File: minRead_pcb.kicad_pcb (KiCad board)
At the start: 2 copper layers, 133.9 x 116.2 mm, 121 parts, among them J1 USB_C_Receptacle, J2 FH34SRJ-24S-0.5SH_50_, J3 FH34SRJ-6S-0.5SH_50_, J5 Conn_01x02, J7 Micro_SD_Card, Q10 BSS138, Q11 BSS138, Q16 MMBT3906, Q17 MMBT3904, Q18 AO3419, Q4 [BSS138] AO3400A, Q5 AO3419, SW1 SW_Push, SW10 SW_Push, SW11 SW_Push, SW2 SW_Push, SW3 SW_Push, SW4 SW_Push, SW6 SW_Push, SW8 SW_Push, SW9 SW_Push, U1 TPD4E1U06DBVR, U11 AP3031KTR, U2 TPS2116DRL, U3 AP2112K-3.3, U4 ESP32-S3-WROOM-1, U6 TPD4E1U06DBVR, U7 MCP73832-2-OT

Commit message: general setup prep for routing
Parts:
- moved J1 133.1 mm to (92.5, 39.7), turned to 0 degrees
- moved J7 114.1 mm to (93.9, 133.2), turned to -90 degrees
- moved U4 102.6 mm to (59.2, 47.7), turned to -135 degrees
- moved R21 99.5 mm to (48.7, 55.9), turned to -135 degrees
- moved R22 98.0 mm to (50.2, 57.4), turned to -135 degrees
- moved R23 96.5 mm to (51.7, 58.9), turned to -135 degrees
- moved R25 95.0 mm to (53.2, 60.4), turned to -135 degrees
- moved R29 94.5 mm to (74.9, 54.5), turned to 135 degrees
- moved R30 93.7 mm to (73.5, 55.9), turned to 135 degrees
- moved R24 93.5 mm to (54.7, 61.9), turned to -135 degrees
- moved R31 93.0 mm to (72.0, 57.2), turned to 135 degrees
- moved R32 92.1 mm to (70.7, 58.7), turned to 135 degrees
- moved R13 91.3 mm to (56.9, 64.1), turned to 45 degrees
- moved R33 91.3 mm to (69.2, 60.1), turned to 135 degrees
- moved R34 90.6 mm to (67.8, 61.5), turned to 135 degrees
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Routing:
- net Net-(U4-IO42): track 0.00 -> 4.34 mm
- net Net-(U4-IO41): track 0.00 -> 3.93 mm
- net ESP32_IO0: track 0.00 -> 3.68 mm
- net Net-(U4-IO40): track 0.00 -> 3.57 mm
- net Net-(U4-IO38): track 0.00 -> 3.43 mm
- net Net-(U4-IO39): track 0.00 -> 3.22 mm
- net Net-(U4-IO9): track 0.00 -> 3.07 mm
- net Net-(U4-IO14): track 0.00 -> 2.96 mm
- net Net-(U4-IO10): track 0.00 -> 2.72 mm
- net Net-(U4-IO13): track 0.00 -> 2.66 mm
- net Net-(U4-IO12): track 0.00 -> 2.35 mm
- net Net-(U4-IO11): track 0.00 -> 2.31 mm
- net Net-(U4-IO48): track 0.00 -> 2.06 mm
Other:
- board size 133.9 x 116.2 mm -> 151.5 x 148.6 mm

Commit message: add specific netclasses
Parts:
- moved R7 102.2 mm to (67.8, 55.6), turned to 90 degrees
- moved C5 100.7 mm to (70.0, 55.6), turned to -90 degrees
- moved C32 100.4 mm to (66.2, 58.6), turned to 0 degrees
- moved C33 99.2 mm to (62.4, 58.6)
- moved R29 18.7 mm to (72.2, 36.0), turned to 180 degrees
- moved R30 17.9 mm to (72.2, 38.0), turned to 180 degrees
- moved R31 17.2 mm to (72.1, 40.0), turned to 180 degrees
- moved R32 16.8 mm to (72.2, 42.0), turned to 180 degrees
- moved R33 16.4 mm to (72.2, 44.0), turned to 180 degrees
- moved R34 16.1 mm to (72.2, 46.0), turned to 180 degrees
- moved R26 15.8 mm to (72.0, 48.2), turned to 0 degrees
- moved R13 12.1 mm to (65.4, 55.5), turned to 90 degrees
- moved R24 10.6 mm to (63.2, 55.5), turned to -90 degrees
- moved R25 9.24 mm to (61.1, 55.5), turned to -90 degrees
- moved R23 7.97 mm to (59.0, 55.5), turned to -90 degrees
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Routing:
- net 3V3: track 0.00 -> 39.3 mm, vias 0 -> 2
- net ESP32_EN: track 0.00 -> 35.2 mm, vias 0 -> 2
- net ESP32_IO0: track 3.68 -> 4.20 mm

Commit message: implement charge pump
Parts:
- removed C25, C26: 1u, Capacitor_SMD:C_0805_2012Metric_Pad1.18x1.45mm_HandSolder
- removed C4: 22u, Capacitor_SMD:C_0805_2012Metric_Pad1.18x1.45mm_HandSolder
- removed R38: 310k, Resistor_SMD:R_0805_2012Metric_Pad1.20x1.40mm_HandSolder
- removed R51, R58: 100k, Resistor_SMD:R_0805_2012Metric_Pad1.20x1.40mm_HandSolder
- removed U2: TPS2116DRL, Package_TO_SOT_SMD:SOT-583-8
- added C7: 22u, Capacitor_SMD:C_0805_2012Metric_Pad1.18x1.45mm_HandSolder, B.Cu at (94.0, 55.0)
- added C9: 4.7u, Capacitor_SMD:C_0805_2012Metric_Pad1.18x1.45mm_HandSolder, B.Cu at (86.2, 53.6)
- added D7: B5819W, Diode_SMD:D_SOD-123, B.Cu at (89.8, 56.2)
- added Q6: AO3419, Package_TO_SOT_SMD:SOT-23_Handsoldering, B.Cu at (85.4, 56.6)
- added R67: 100k, Resistor_SMD:R_0805_2012Metric_Pad1.20x1.40mm_HandSolder, B.Cu at (92.0, 55.0)
- J5: footprint Connector_JST:JST_PH_S2B-PH-K_1x02_P2.00mm_Horizontal -> DEAN:Battery pads
- moved C19 163.4 mm to (71.6, 132.6), turned to 90 degrees
- moved C18 160.6 mm to (69.6, 132.6), turned to 90 degrees
- moved C14 159.4 mm to (75.6, 132.6), turned to 90 degrees
- moved C17 156.1 mm to (65.6, 132.6), turned to 90 degrees
- moved R14 153.5 mm to (76.8, 156.4)
- moved C20 151.6 mm to (81.6, 132.6), turned to 90 degrees
- moved C16 151.0 mm to (79.6, 132.6), turned to 90 degrees
- moved Q4 150.5 mm to (74.0, 156.5), turned to -90 degrees
- moved C15 150.5 mm to (77.6, 132.6), turned to 90 degrees
- moved R15 150.0 mm to (71.2, 156.6)
- moved C13 148.4 mm to (73.6, 132.6), turned to 90 degrees
- moved C6 146.5 mm to (96.2, 59.2), turned to 90 degrees
- moved R12 141.2 mm to (73.8, 57.1), turned to 90 degrees
- moved L1 139.8 mm to (68.0, 156.6)
- moved U3 139.4 mm to (93.4, 59.8), turned to -90 degrees
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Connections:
- U4 pad 6: WARM_TOGGLE -> COLOR_SEL
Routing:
- net BAT_MONIT: track 0.00 -> 34.6 mm
- net ESP32_EN: track 35.2 -> 2.22 mm, vias 2 -> 0
- net P+: track 0.00 -> 25.0 mm
- net B-: track 0.00 -> 24.1 mm, vias 0 -> 1
- net LDO_IN: track 0.00 -> 11.1 mm
- net Net-(C18-Pad2): track 0.00 -> 10.7 mm
- net 3V3: track 39.3 -> 49.6 mm
- net USB_VBUS: track 0.00 -> 9.89 mm
- net Net-(D5-A): track 0.00 -> 9.18 mm
- net Net-(C19-Pad2): track 0.00 -> 9.17 mm
- net Net-(C13-Pad2): track 0.00 -> 7.70 mm
- net Net-(C17-Pad2): track 0.00 -> 7.61 mm
- net Net-(C20-Pad2): track 0.00 -> 7.34 mm
- net /PREVGH: track 0.00 -> 6.40 mm
- net Net-(D4-K): track 0.00 -> 6.00 mm
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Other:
- outline, holes or cut-outs redrawn

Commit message: charge pump in place
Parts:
- moved R15 22.5 mm to (83.0, 137.4)
- moved C10 20.0 mm to (71.2, 137.6)
- moved D6 20.0 mm to (62.2, 138.0)
- moved L1 20.0 mm to (74.4, 137.6)
- moved C11 20.0 mm to (66.8, 138.0)
- moved D4 20.0 mm to (64.6, 138.0)
- moved D5 20.0 mm to (69.0, 137.8)
- moved Q4 19.4 mm to (78.2, 137.5)
- moved R14 19.4 mm to (81.0, 137.4)
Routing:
- net /GDR: track 1.85 -> 6.65 mm
- net Net-(D5-A): track 9.18 -> 5.43 mm
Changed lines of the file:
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@@
 	(footprint "Capacitor_SMD:C_0805_2012Metric_Pad1.18x1.45mm_HandSolder"
 		(layer "B.Cu")
-		(at 64.8 156.5625 -90)
+		(at 71.2 137.6 -90)
 		(descr "Capacitor SMD 0805 (2012 Metric), square (rectangular) end terminal, IPC-7351 nominal with elongated pad for handsoldering. (Body size source: IPC-SM-782 page 76, https://www.pcb-3d.com/wordpress/wp-content/uploads/ipc-sm-782a_amendment_1_and_2.pdf, https://docs.google.com/spreadsheets/d/1BsfQQcO9C6DZCsRaXUlFlo91Tg2WpOkGARC1WS5S8t0/edit?usp=sharing), generated with kicad-footprint-generator")
 		(tags "capacitor handsolder")
@@
 	(footprint "Capacitor_SMD:C_0805_2012Metric_Pad1.18x1.45mm_HandSolder"
 		(layer "B.Cu")
-		(at 60.4 156.9625 -90)
+		(at 66.8 138 -90)
 		(descr "Capacitor SMD 0805 (2012 Metric), square (rectangular) end terminal, IPC-7351 nominal with elongated pad for handsoldering. (Body size source: IPC-SM-782 page 76, https://www.pcb-3d.com/wordpress/wp-content/uploads/ipc-sm-782a_amendment_1_and_2.pdf, https://docs.google.com/spreadsheets/d/1BsfQQcO9C6DZCsRaXUlFlo91Tg2WpOkGARC1WS5S8t0/edit?usp=sharing), generated with kicad-footprint-generator")
 		(tags "capacitor handsolder")
@@
 	(footprint "Package_TO_SOT_SMD:SOT-23"
 		(layer "B.Cu")
-		(at 74 156.5 -90)
+		(at 78.2 137.5375 -90)
 		(descr "SOT, 3 Pin (JEDEC TO-236 Var AB https://www.jedec.org/document_search?search_api_views_fulltext=TO-236), generated with kicad-footprint-generator ipc_gullwing_generator.py")
 		(tags "SOT TO_SOT_SMD")
@@
 	(footprint "Resistor_SMD:R_0805_2012Metric_Pad1.20x1.40mm_HandSolder"
 		(layer "B.Cu")
-		(at 71.2 156.5625 90)
+		(at 83 137.4375 90)
 		(descr "Resistor SMD 0805 (2012 Metric), square (rectangular) end terminal, IPC-7351 nominal with elongated pad for handsoldering. (Body size source: IPC-SM-782 page 72, https://www.pcb-3d.com/wordpress/wp-content/uploads/ipc-sm-782a_amendment_1_and_2.pdf), generated with kicad-footprint-generator")
 		(tags "resistor handsolder")
@@
 	(footprint "Diode_SMD:D_SOD-123"
 		(layer "B.Cu")
-		(at 55.8 156.9625 -90)
+		(at 62.2 138 -90)
 		(descr "SOD-123")
 		(tags "SOD-123")
@@
 	(footprint "Diode_SMD:D_SOD-123"
 		(layer "B.Cu")
-		(at 62.6 156.7625 -90)
+		(at 69 137.8 -90)
 		(descr "SOD-123")
 		(tags "SOD-123")
@@
 	(footprint "Resistor_SMD:R_0805_2012Metric_Pad1.20x1.40mm_HandSolder"
 		(layer "B.Cu")
-		(at 76.8 156.3625 90)
+		(at 81 137.4375 90)
 		(descr "Resistor SMD 0805 (2012 Metric), square (rectangular) end terminal, IPC-7351 nominal with elongated pad for handsoldering. (Body size source: IPC-SM-782 page 72, https://www.pcb-3d.com/wordpress/wp-content/uploads/ipc-sm-782a_amendment_1_and_2.pdf), generated with kicad-footprint-generator")
 		(tags "resistor handsolder")
@@
 	(footprint "Diode_SMD:D_SOD-123"
 		(layer "B.Cu")
-		(at 58.2 156.9625 90)
+		(at 64.6 138 90)
 		(descr "SOD-123")
 		(tags "SOD-123")
@@
 	(footprint "srn3010C-100m:IND_SRN3010C-100M"
 		(layer "B.Cu")
-		(at 68 156.5625 180)
+		(at 74.4 137.6 180)
 		(property "Reference" "L1"
 			(at 0 2.25 0)
@@
 	)
 	(segment
-		(start 64.8 157.6)
-		(end 65.8625 157.6)
+		(start 71.2 138.6375)
+		(end 72.2625 138.6375)
 		(width 0.5)
 		(layer "B.Cu")
@@
 	)
 	(segment
-		(start 65.8625 157.6)
-		(end 66.9 156.5625)
+		(start 72.2625 138.6375)
+		(end 73.3 137.6)
 		(width 0.5)
 		(layer "B.Cu")
@@
 	)
 	(segment
-		(start 60.4 155.925)
-		(end 58.2 158.125)
+		(start 66.8 136.9625)
+		(end 64.6 139.1625)
 		(width 0.5)
 		(layer "B.Cu")
@@
 	)
 	(segment
-		(start 58.2 158.125)
-		(end 58.2 158.6125)
+		(start 64.6 139.1625)
+		(end 64.6 139.65)
 		(width 0.5)
 		(layer "B.Cu")
@@
 	)
 	(segment
-		(start 55.8 158.6125)
-		(end 58.2 158.6125)
+		(start 62.2 139.65)
+		(end 64.6 139.65)
 		(width 0.5)
 		(layer "B.Cu")
@@
 	)
 	(segment
-		(start 62.6 158.4125)
-		(end 60.8125 158.4125)
+		(start 69 139.45)
+		(end 67.2125 139.45)
 		(width 0.5)
 		(layer "B.Cu")
@@
 	)
 	(segment
-		(start 60.8125 158.4125)
-		(end 60.4 158)
+		(start 67.2125 139.45)
+		(end 66.8 139.0375)
 		(width 0.5)
 		(layer "B.Cu")
@@
 	)
 	(segment
-		(start 69.1 157.400798)
-		(end 69.1 156.5625)
+		(start 76.375 138.475)
+		(end 78.2 138.475)
 		(width 0.5)
 		(layer "B.Cu")
@@
 	)
 	(segment
-		(start 72.725 158.7125)
-		(end 70.411702 158.7125)
-		(width 0.5)
-		(layer "B.Cu")
-		(net "Net-(D5-A)")
-	)
-	(segment
-		(start 70.411702 158.7125)
-		(end 69.1 157.400798)
-		(width 0.5)
-		(layer "B.Cu")
-		(net "Net-(D5-A)")
-	)
-	(segment
-		(start 74 157.4375)
-		(end 72.725 158.7125)
+		(start 75.5 137.6)
+		(end 76.375 138.475)
 		(width 0.5)
 		(layer "B.Cu")
@@
 	)
 	(segment
-		(start 73.05 155.5625)
-		(end 71.2 155.5625)
+		(start 78.4125 135.4375)
+		(end 77.25 136.6)
+		(width 0.2)
+		(layer "B.Cu")
+		(net "/GDR")
+	)
+	(segment
+		(start 83 136.4375)
+		(end 82 135.4375)
+		(width 0.2)
+		(layer "B.Cu")
+		(net "/GDR")
+	)
+	(segment
+		(start 82 135.4375)
+		(end 78.4125 135.4375)
 		(width 0.2)
 		(layer "B.Cu")
@@
 	)
 	(segment
-		(start 76.8 155.3625)
-		(end 75.15 155.3625)
+		(start 81 136.4)
+		(end 79.35 136.4)
 		(width 0.5)
 		(layer "B.Cu")
@@
 	)
 	(segment
-		(start 75.15 155.3625)
-		(end 74.95 155.5625)
+		(start 79.35 136.4)
+		(end 79.15 136.6)
 		(width 0.5)
 		(layer "B.Cu")

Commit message: light bar circuit mostly routed
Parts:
- moved R48 257.9 mm to (49.0, 137.8), turned to -90 degrees
- moved R47 249.2 mm to (57.9, 138.1), turned to -90 degrees
- moved Q17 245.0 mm to (51.7, 137.0), turned to 90 degrees
- moved Q16 241.4 mm to (55.2, 137.0), turned to 90 degrees
- moved R63 180.4 mm to (49.9, 132.3), turned to -90 degrees
- moved R62 174.9 mm to (58.7, 132.3), turned to -90 degrees
- moved C30 170.7 mm to (59.1, 135.2), turned to 0 degrees
- moved Q10 163.9 mm to (56.0, 132.3), turned to 90 degrees
- moved Q11 163.8 mm to (52.5, 132.3), turned to 90 degrees
- moved R65 154.7 mm to (47.2, 66.4)
- moved C34 151.9 mm to (44.4, 61.9), turned to 90 degrees
- moved R64 150.9 mm to (51.3, 64.6)
- moved C31 147.8 mm to (48.4, 58.0), turned to -90 degrees
- moved R5 146.4 mm to (65.6, 132.6), turned to -90 degrees
- moved Q18 144.3 mm to (47.2, 62.7), turned to 90 degrees
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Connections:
- U4 pad 10: LED_PWR -> LED_ACTIVATE
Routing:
- net LED_SW: track 0.00 -> 77.9 mm
- net EPD_MOSI: track 0.00 -> 35.0 mm, vias 0 -> 2
- net EPD_SCK: track 0.00 -> 33.1 mm, vias 0 -> 2
- net EPD_CS: track 0.00 -> 32.0 mm, vias 0 -> 2
- net EPD_DC: track 0.00 -> 31.0 mm, vias 0 -> 2
- net EPD_BUSY: track 0.00 -> 29.1 mm, vias 0 -> 2
- net /RESE: track 1.93 -> 19.6 mm
- net /GDR: track 6.65 -> 21.5 mm
- net COLOR_SEL: track 0.00 -> 13.6 mm, vias 0 -> 2
- net C-: track 0.00 -> 11.0 mm, vias 0 -> 2
- net Net-(D10-A): track 0.00 -> 10.9 mm
- net /PREVGL: track 5.80 -> 16.6 mm
- net W-: track 0.00 -> 10.1 mm, vias 0 -> 2
- net 3V3: track 49.6 -> 59.6 mm
- net EPD_RST: track 0.00 -> 9.36 mm
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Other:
- outline, holes or cut-outs redrawn

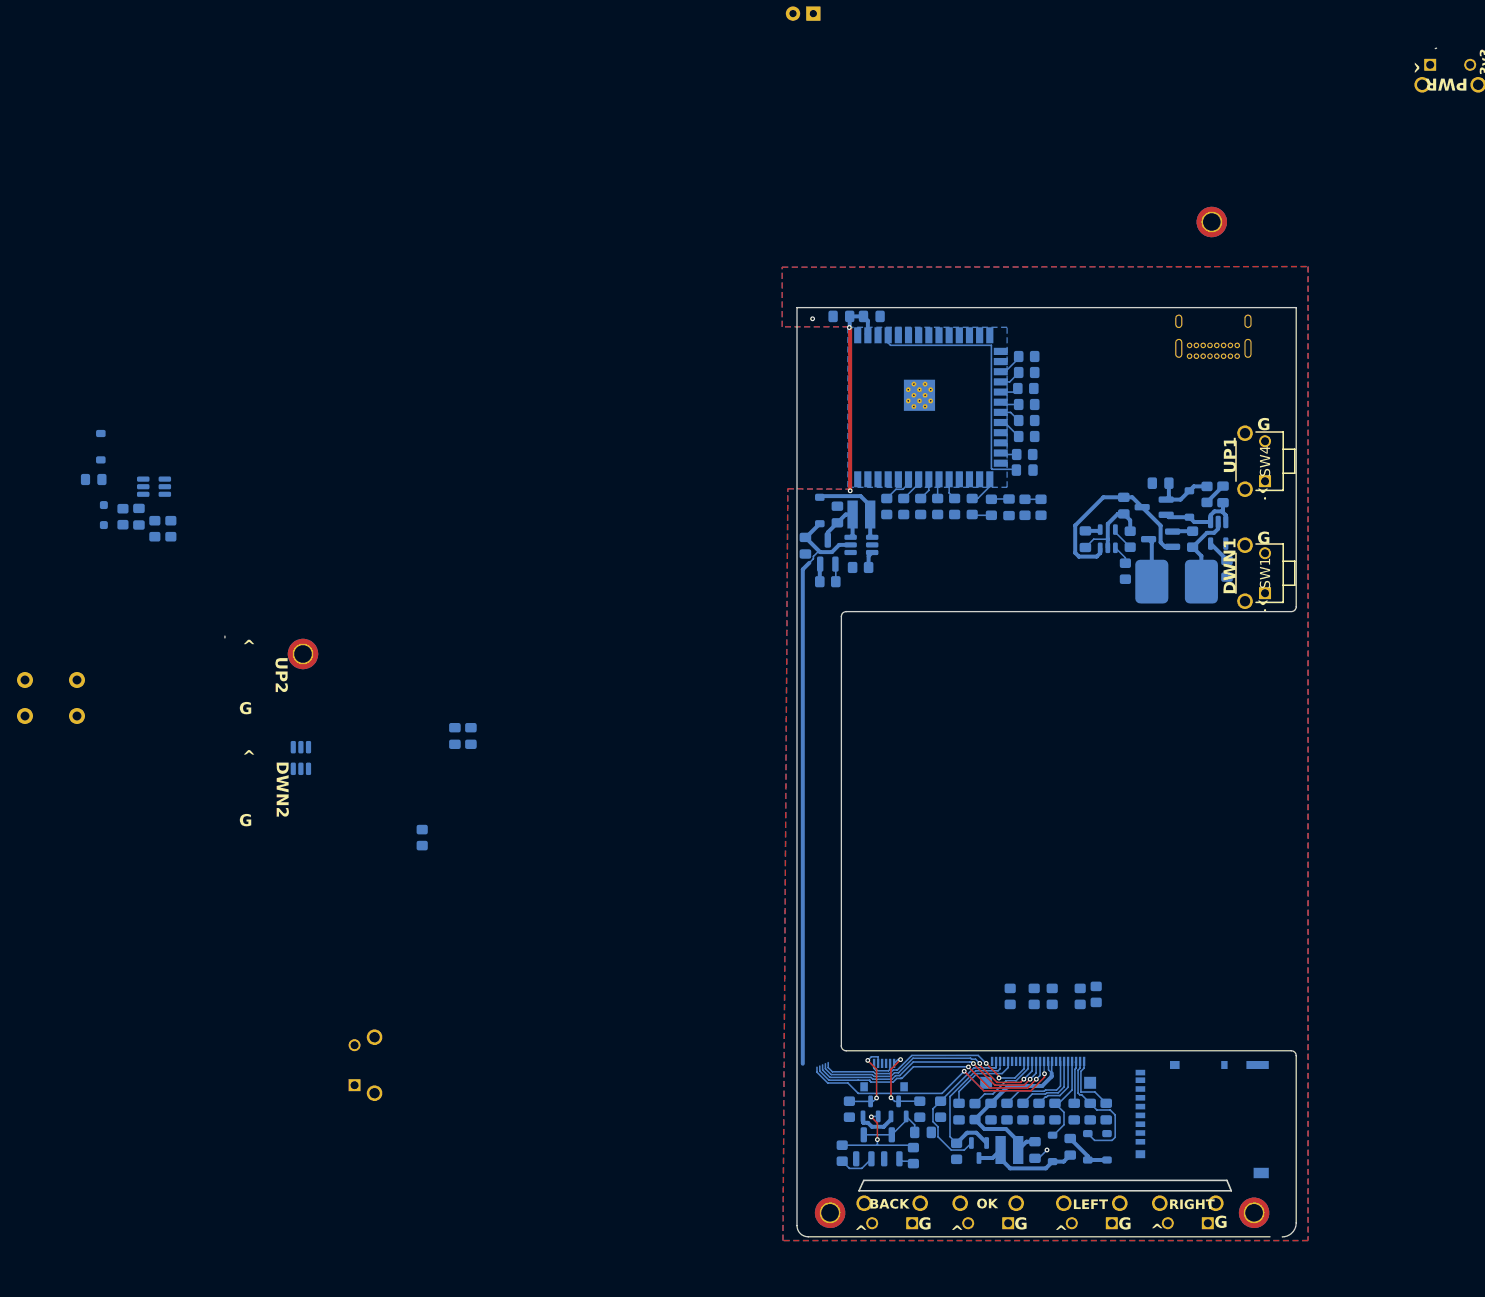
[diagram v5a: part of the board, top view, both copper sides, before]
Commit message: reverse mount buttons
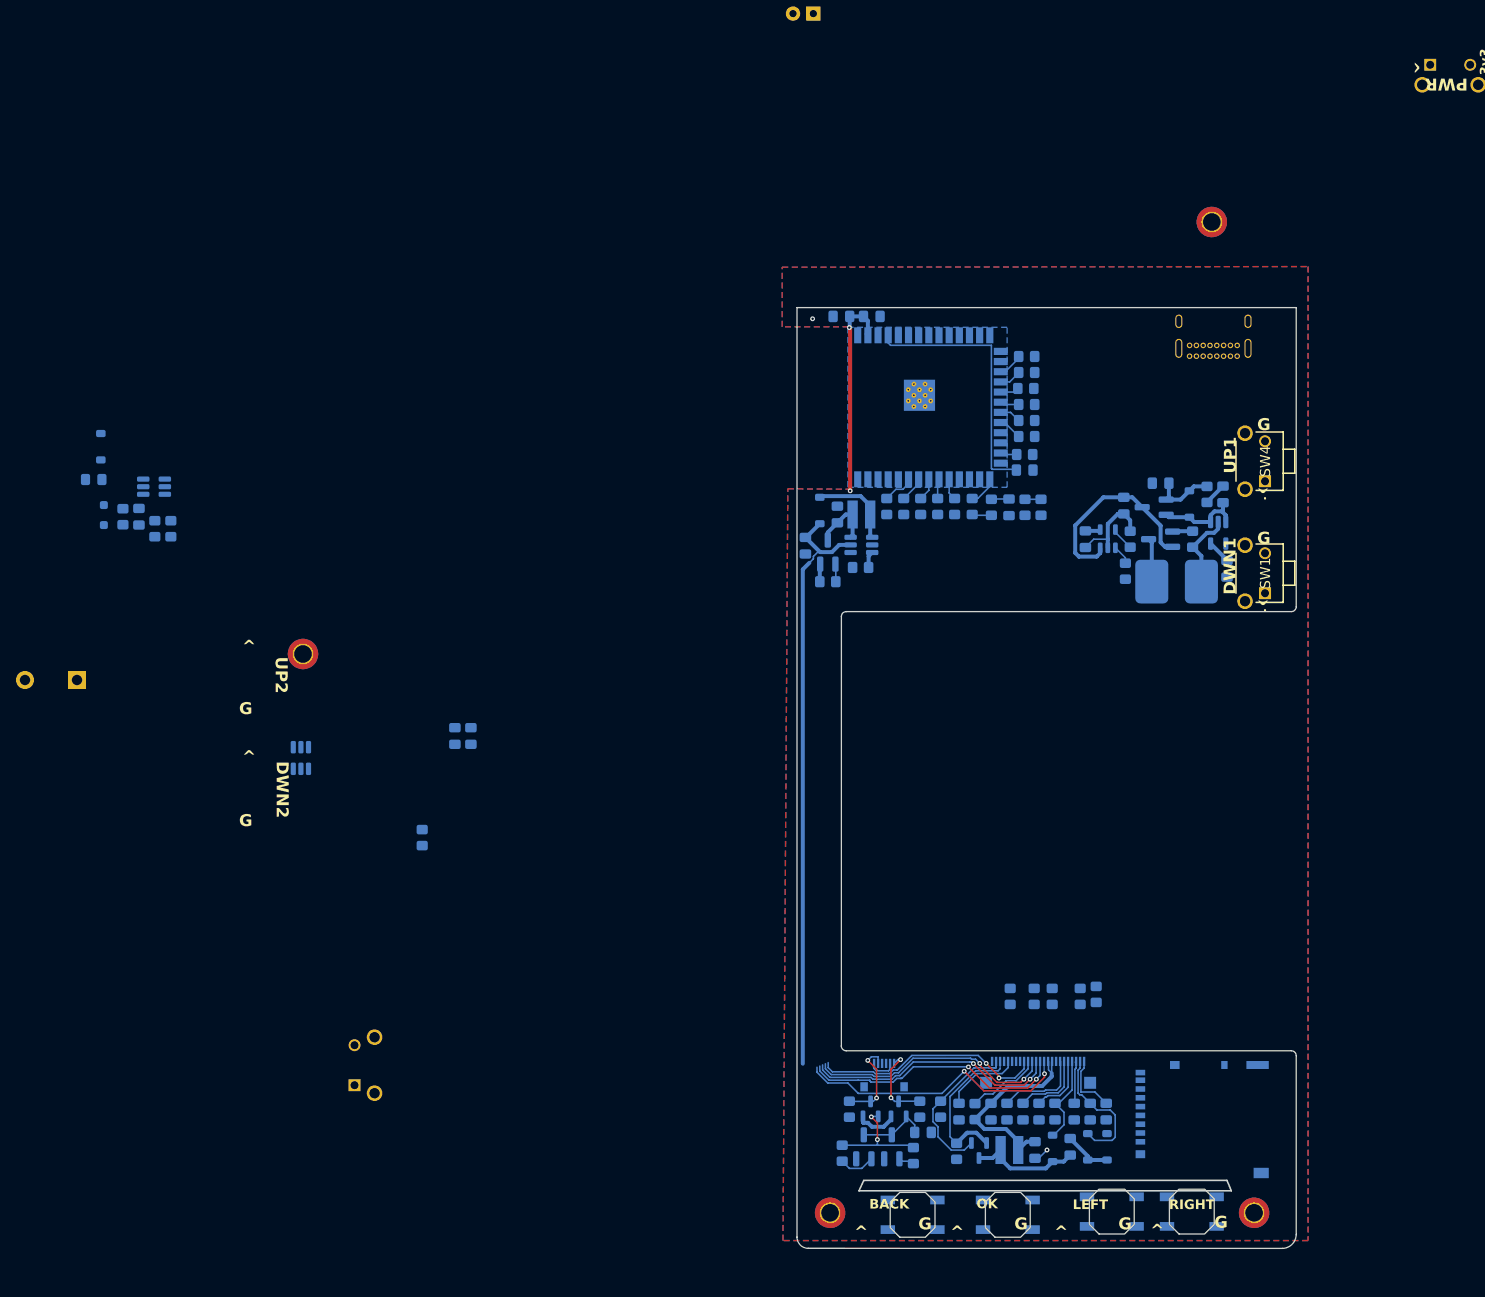
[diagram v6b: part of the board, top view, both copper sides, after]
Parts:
- SW2, SW3, SW8, SW9: footprint mjtp1117:MJTP1117 -> DEAN:SKQGABE010_ALPS_Reverse
- SW6: footprint Button_Switch_THT:SW_PUSH_6mm -> Button_Switch_THT:SW_PUSH_1P1T_6x3.5mm_H4.3_APEM_MJTP1243
- moved SW2 2.47 mm to (92.7, 145.1)
- moved SW3 1.46 mm to (82.7, 145.1)
- moved SW8 1.06 mm to (69.7, 145.5)
- moved SW9 1.06 mm to (57.8, 145.5)
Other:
- board size 151.5 x 148.6 mm -> 62.4 x 117.6 mm
